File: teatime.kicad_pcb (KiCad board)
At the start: 2 copper layers, 100 x 100 mm, 85 parts, among them SW1 SW_Push, U1 MCP1700-3302E, U2 74HC595, U3 74HC595, U4 74HC595, U5 74HC595, U6 ATtiny85-20PU

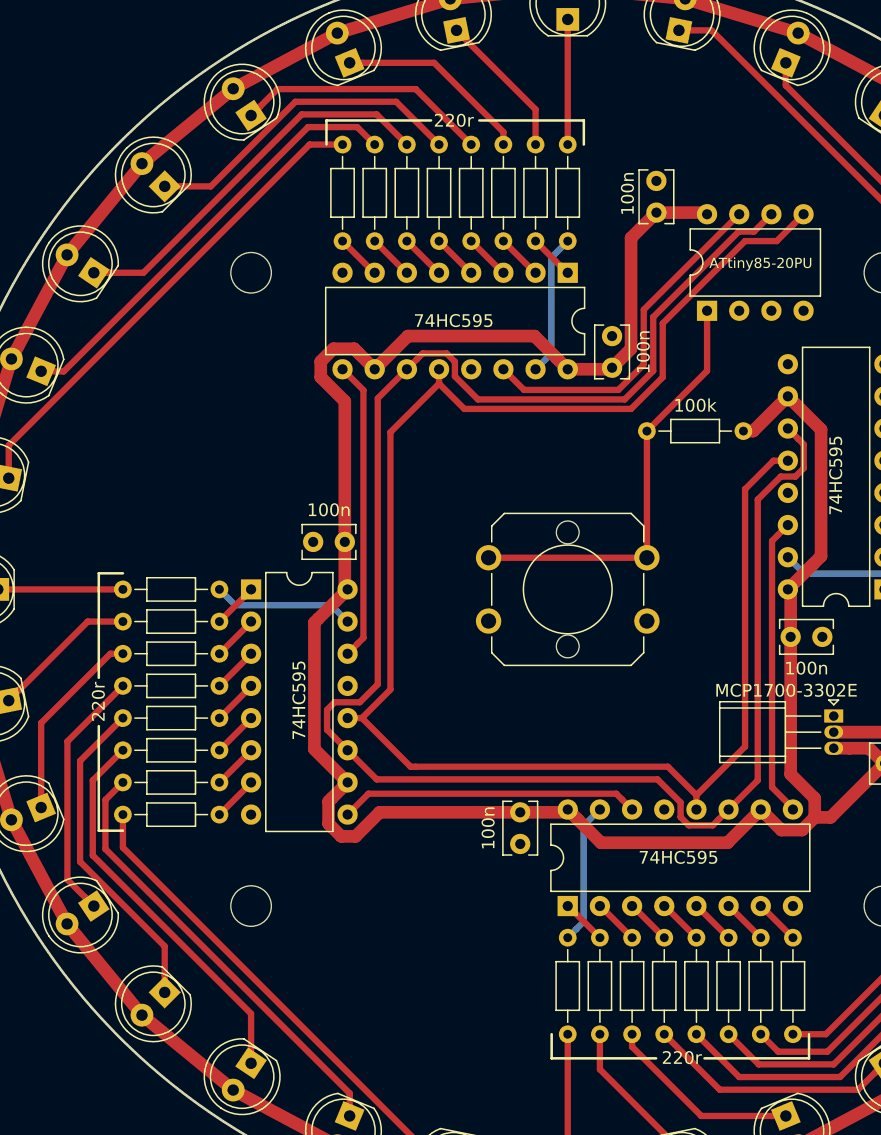
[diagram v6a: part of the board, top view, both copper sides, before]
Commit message: More updates, added buzzer
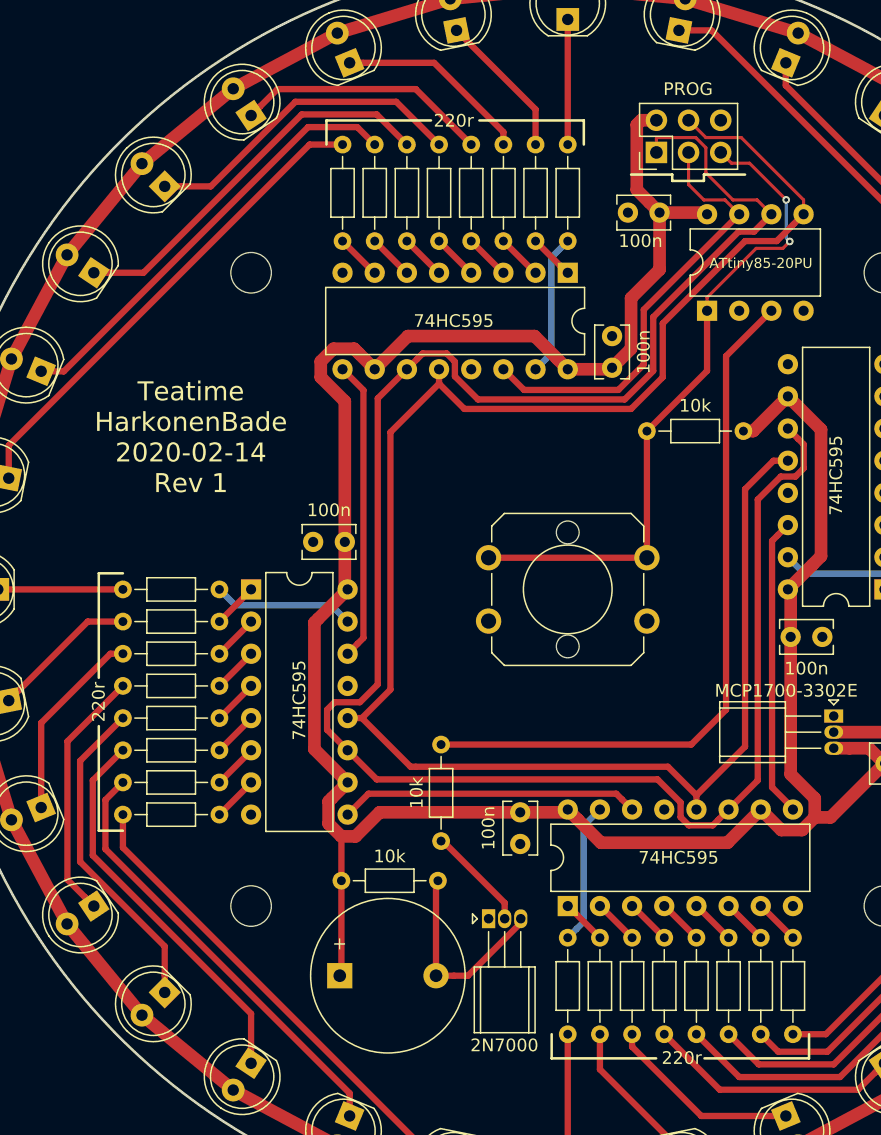
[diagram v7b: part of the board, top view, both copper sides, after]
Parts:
- added J1: PROG, Connector_PinHeader_2.54mm:PinHeader_2x03_P2.54mm_Vertical, F.Cu at (107.0, 65.5)
- added LS1: Speaker, Buzzer_Beeper:Buzzer_12x9.5RM7.6, F.Cu at (82.0, 130.5)
- added Q1: 2N7000, Package_TO_SOT_THT:TO-92_Inline_W4.0mm_Horizontal_FlatSideDown, F.Cu at (93.8, 126.0)
- added R34: 10k, Resistor_THT:R_Axial_DIN0204_L3.6mm_D1.6mm_P7.62mm_Horizontal, F.Cu at (89.8, 123.0)
- added R35: 10k, Resistor_THT:R_Axial_DIN0204_L3.6mm_D1.6mm_P7.62mm_Horizontal, F.Cu at (90.0, 112.2)
- R33: value 100k -> 10k
- moved C3 0.25 mm to (107.2, 70.2), turned to 180 degrees
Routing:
- net Net-(R35-Pad1): track 0.00 -> 56.6 mm
- net +3V3: track 505.2 -> 525.5 mm
- net Net-(J1-Pad5): track 34.0 -> 53.5 mm, vias 0 -> 2
- net Net-(LS1-Pad2): track 0.00 -> 16.3 mm
- net Net-(J1-Pad1): track 142.0 -> 155.9 mm
- net Net-(J1-Pad4): track 129.8 -> 142.6 mm
- net Net-(Q1-Pad2): track 0.00 -> 8.29 mm
- net Net-(J1-Pad3): track 27.6 -> 35.1 mm
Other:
- board text removed: "github.com/HarkonenBade/teatime"
